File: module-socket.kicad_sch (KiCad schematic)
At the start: 3 parts, among them CON1 MIKROBUS_HOST_CONN

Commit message: Updated MCU to MCU module + set SMD comp. footprints
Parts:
- C36, C37: footprint (none) -> Capacitor_SMD:C_0603_1608Metric
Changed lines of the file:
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@@
 			)
 		)
-		(property "Footprint" ""
+		(property "Footprint" "Capacitor_SMD:C_0603_1608Metric"
 			(at 103.8352 109.22 0)
 			(effects
@@
 			)
 		)
-		(property "Footprint" ""
+		(property "Footprint" "Capacitor_SMD:C_0603_1608Metric"
 			(at 166.0652 109.22 0)
 			(effects

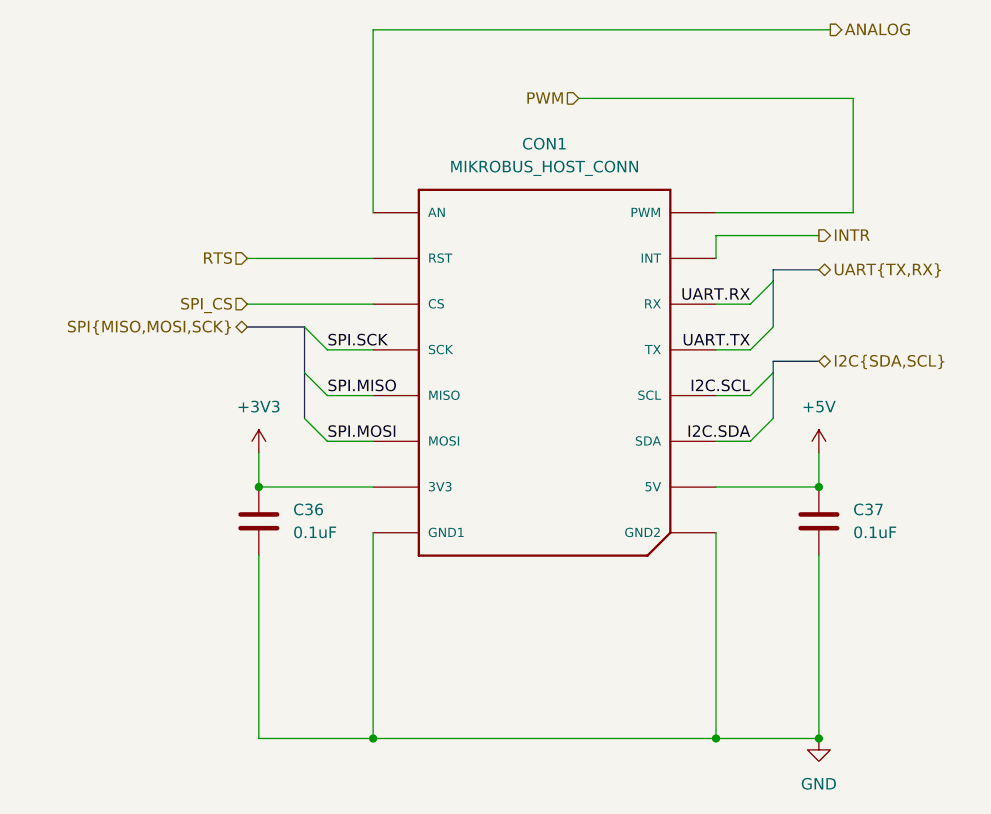
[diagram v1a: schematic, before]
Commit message: finished routing SPI, I2C and MikroBUS
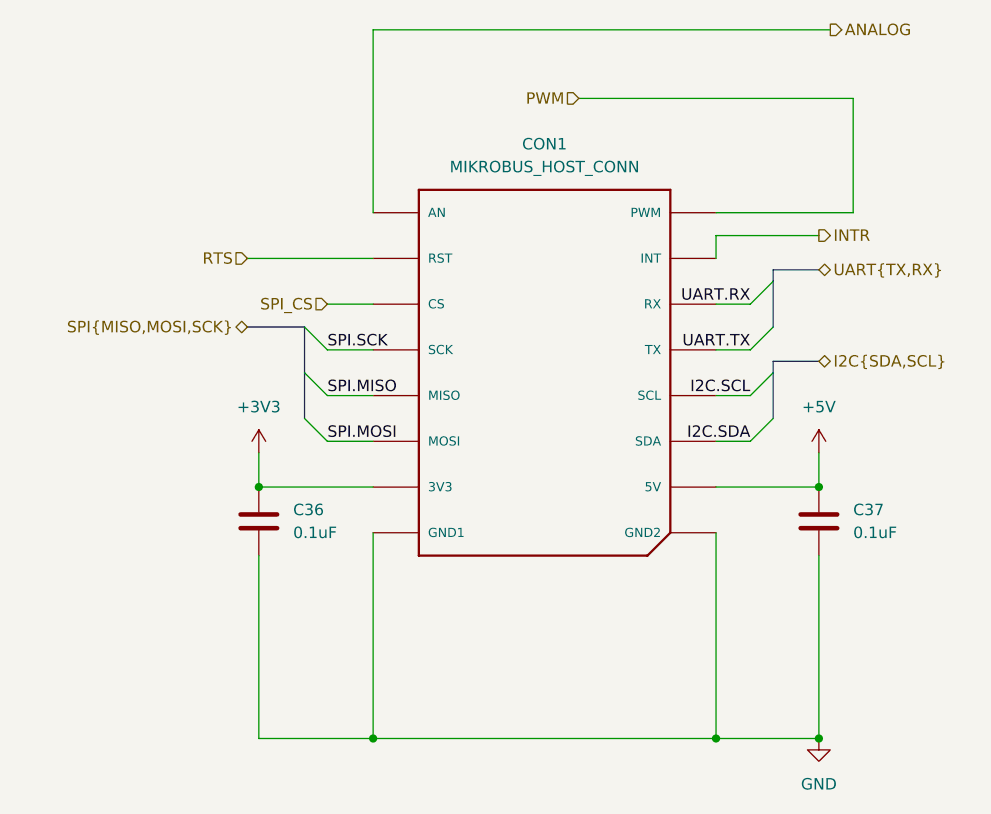
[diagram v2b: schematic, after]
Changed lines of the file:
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@@
 	(wire
 		(pts
-			(xy 101.6 81.28) (xy 115.57 81.28)
+			(xy 110.49 81.28) (xy 115.57 81.28)
 		)
 		(stroke
@@
 	(hierarchical_label "SPI_CS"
 		(shape input)
-		(at 101.6 81.28 180)
-		(effects
-			(font
+		(at 110.49 81.28 180)
+		(effects
+			(font
